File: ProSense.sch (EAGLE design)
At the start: 26 parts, among them U4 MIC2505 3.3

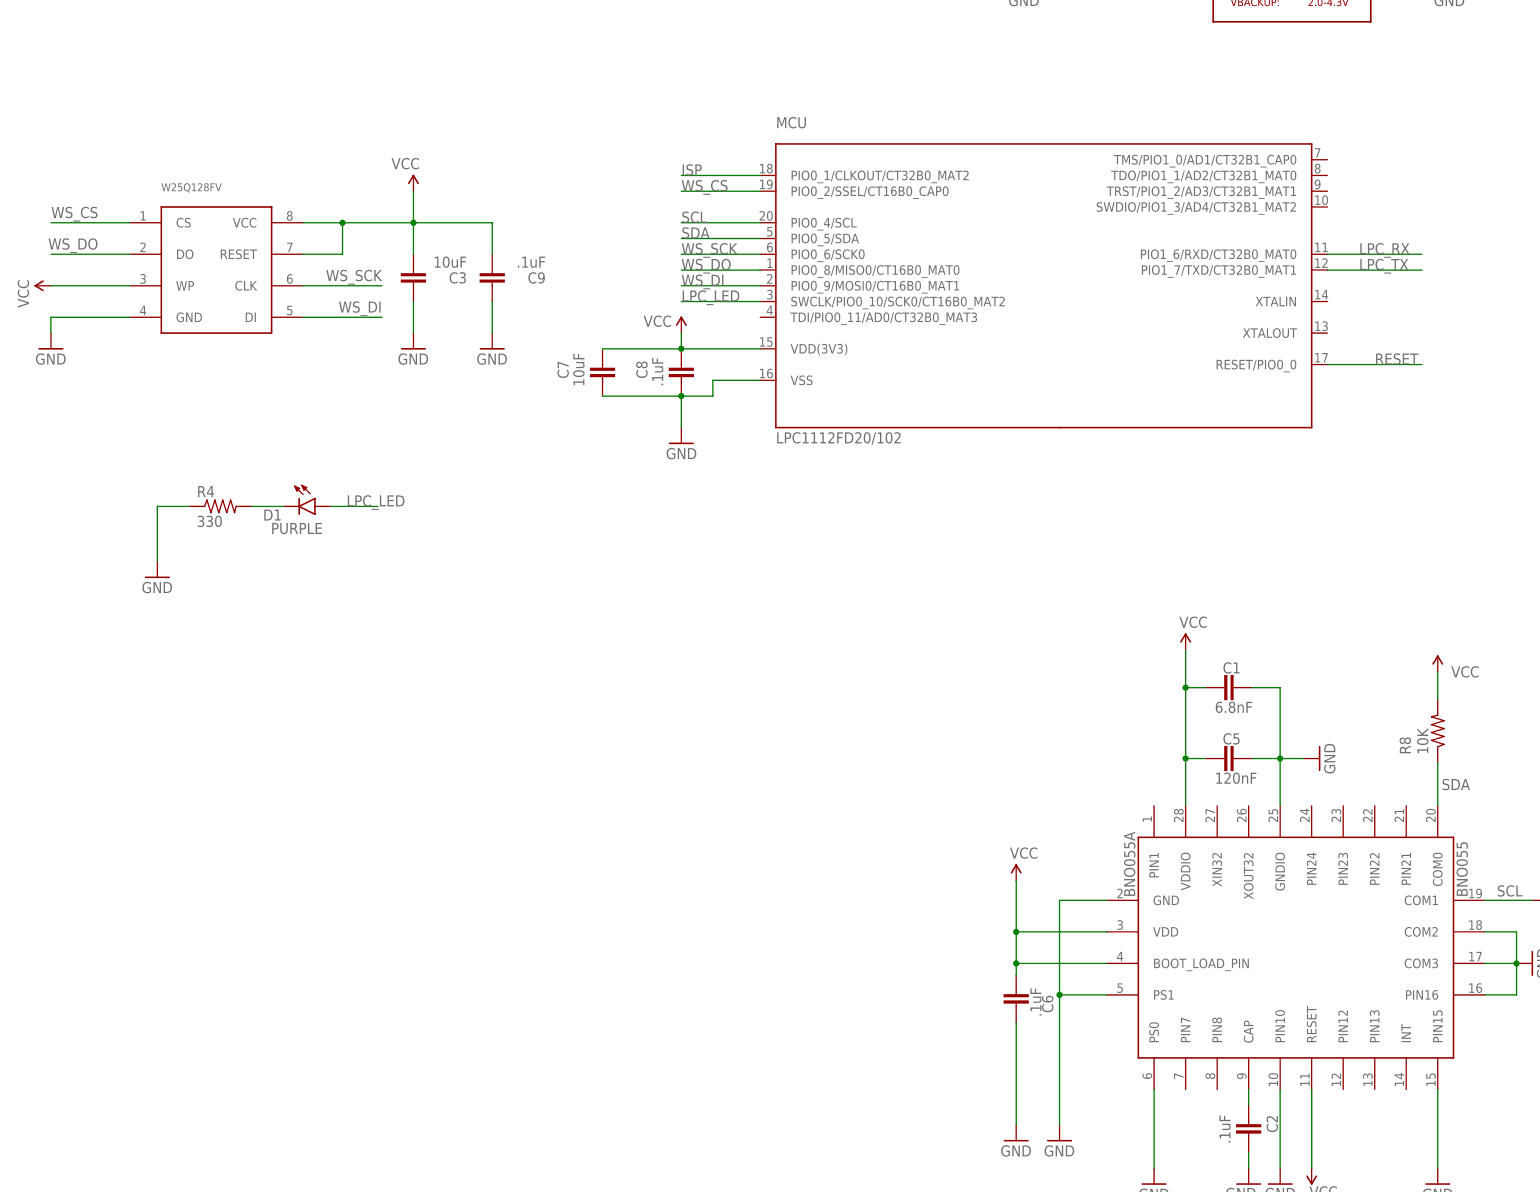
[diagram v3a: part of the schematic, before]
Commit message: Initial commit for QFN Package
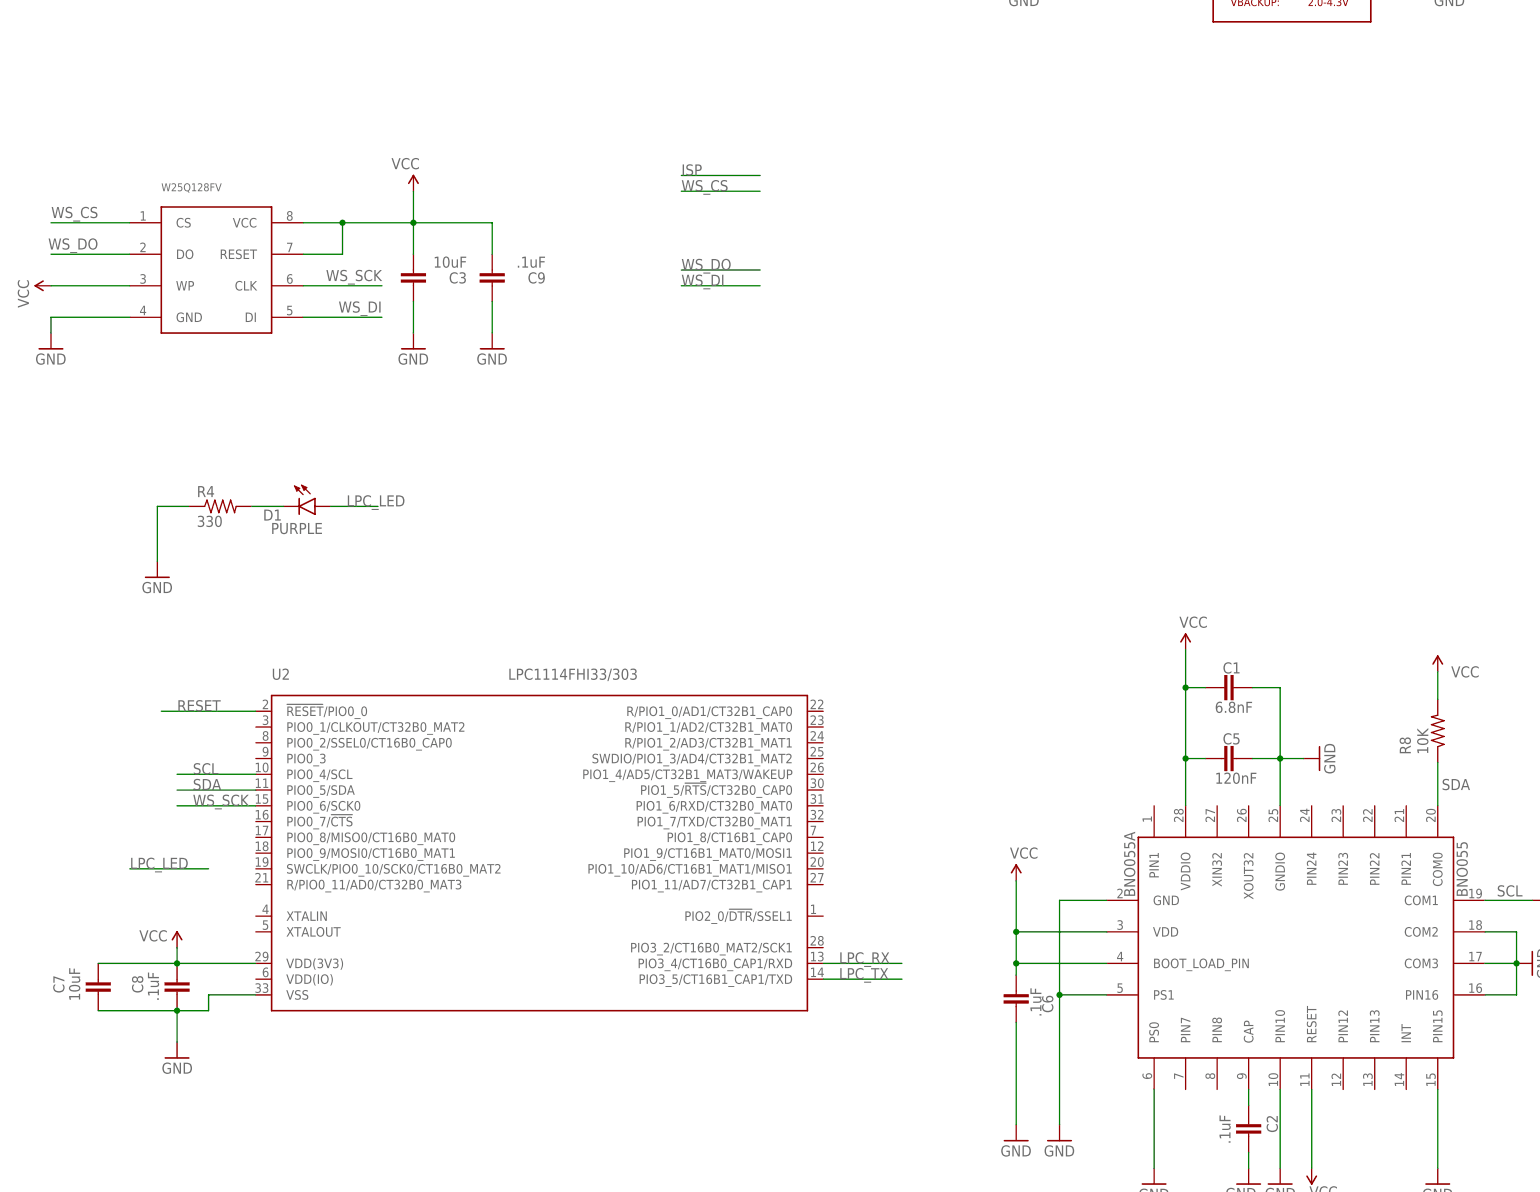
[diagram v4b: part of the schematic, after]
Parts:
- removed MCU: LPC1112FD20/102, NXP_60_26022015:LPC1112FD20/102
- added U2: LPC1114FHI33/303, NXP_60_26022015:LPC1114FHI33/303
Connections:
- net GND: now also U2.VSS; no longer MCU.VSS
- net ISP: no longer MCU.PIO0_1/CLKOUT/CT32B0_MAT2
- net LPC_LED: no longer MCU.SWCLK/PIO0_10/SCK0/CT16B0_MAT2
- net LPC_RX: now also U2.PIO3_4/CT16B0_CAP1/RXD; no longer MCU.PIO1_6/RXD/CT32B0_MAT0
- net LPC_TX: now also U2.PIO3_5/CT16B1_CAP1/TXD; no longer MCU.PIO1_7/TXD/CT32B0_MAT1
- net RESET: now also U2.!RESET!/PIO0_0; no longer MCU.RESET/PIO0_0
- net SCL: now also U2.PIO0_4/SCL; no longer MCU.PIO0_4/SCL
- net SDA: now also U2.PIO0_5/SDA; no longer MCU.PIO0_5/SDA
- net VCC: now also U2.VDD(3V3); no longer MCU.VDD(3V3)
- net WS_CS: no longer MCU.PIO0_2/SSEL/CT16B0_CAP0
- net WS_DI: no longer MCU.PIO0_9/MOSI0/CT16B0_MAT1
- net WS_DO: no longer MCU.PIO0_8/MISO0/CT16B0_MAT0
- net WS_SCK: now also U2.PIO0_6/SCK0; no longer MCU.PIO0_6/SCK0
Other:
- moved on the sheet: C7, C8
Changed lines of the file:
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@@
 <setting verticaltext="up"/>
 </settings>
-<grid distance="0.005" unitdist="inch" unit="inch" style="lines" multiple="1" display="no" altdistance="0.01" altunitdist="inch" altunit="inch"/>
+<grid distance="0.1" unitdist="inch" unit="inch" style="lines" multiple="1" display="no" altdistance="0.01" altunitdist="inch" altunit="inch"/>
 <layers>
 <layer number="1" name="Top" color="4" fill="1" visible="no" active="no"/>
@@
 <part name="SUPPLY1" library="SparkFun-Aesthetics" deviceset="V_BATT" device=""/>
 <part name="SUPPLY18" library="SparkFun-Aesthetics" deviceset="VCC" device=""/>
-<part name="MCU" library="NXP_60_26022015" deviceset="LPC1112FD20" device="" technology="/102"/>
 <part name="GND7" library="SparkFun-Aesthetics" deviceset="GND" device=""/>
 <part name="SUPPLY13" library="SparkFun-Aesthetics" deviceset="VCC" device=""/>
@@
 <part name="C9" library="SparkFun-Passives" deviceset="CAP" device="0805" value=".1uF"/>
 <part name="GND12" library="SparkFun-Aesthetics" deviceset="GND" device=""/>
+<part name="U2" library="NXP_60_26022015" deviceset="LPC1114FHI33/303" device=""/>
 </parts>
 <sheets>
@@
 <attribute name="VALUE" x="85.979" y="45.339" size="1.778" layer="96" rot="MR180"/>
 </instance>
-<instance part="C8" gate="G$1" x="-38.1" y="91.44" smashed="yes" rot="MR0">
-<attribute name="NAME" x="-45.339" y="91.694" size="1.778" layer="95" rot="MR90"/>
-<attribute name="VALUE" x="-42.799" y="90.424" size="1.778" layer="96" rot="MR90"/>
-</instance>
-<instance part="GND28" gate="1" x="-38.1" y="81.28" rot="MR0"/>
-<instance part="SUPPLY9" gate="G$1" x="-38.1" y="99.06" smashed="yes" rot="MR0">
-<attribute name="VALUE" x="-39.624" y="100.076" size="1.778" layer="96" rot="MR0"/>
+<instance part="C8" gate="G$1" x="-119.38" y="-7.62" smashed="yes" rot="MR0">
+<attribute name="NAME" x="-126.619" y="-7.366" size="1.778" layer="95" rot="MR90"/>
+<attribute name="VALUE" x="-124.079" y="-8.636" size="1.778" layer="96" rot="MR90"/>
+</instance>
+<instance part="GND28" gate="1" x="-119.38" y="-17.78" rot="MR0"/>
+<instance part="SUPPLY9" gate="G$1" x="-119.38" y="0" smashed="yes" rot="MR0">
+<attribute name="VALUE" x="-120.904" y="1.016" size="1.778" layer="96" rot="MR0"/>
 </instance>
 <instance part="SUPPLY11" gate="G$1" x="-81.28" y="121.92" rot="MR0"/>
@@
 <instance part="SUPPLY1" gate="G$1" x="154.94" y="81.28"/>
 <instance part="SUPPLY18" gate="G$1" x="-139.7" y="106.68" rot="MR270"/>
-<instance part="MCU" gate="G$1" x="20.32" y="106.68"/>
 <instance part="GND7" gate="1" x="-46.355" y="163.195" smashed="yes">
 <attribute name="VALUE" x="-48.895" y="161.29" size="1.27" layer="96"/>
@@
 </instance>
 <instance part="SUPPLY7" gate="G$1" x="43.18" y="48.006"/>
-<instance part="C7" gate="G$1" x="-50.8" y="91.44" smashed="yes" rot="MR0">
-<attribute name="NAME" x="-58.039" y="91.694" size="1.778" layer="95" rot="MR90"/>
-<attribute name="VALUE" x="-55.499" y="90.424" size="1.778" layer="96" rot="MR90"/>
+<instance part="C7" gate="G$1" x="-132.08" y="-7.62" smashed="yes" rot="MR0">
+<attribute name="NAME" x="-139.319" y="-7.366" size="1.778" layer="95" rot="MR90"/>
+<attribute name="VALUE" x="-136.779" y="-8.636" size="1.778" layer="96" rot="MR90"/>
 </instance>
 <instance part="C9" gate="G$1" x="-68.58" y="109.22" smashed="yes" rot="R180">
@@
 </instance>
 <instance part="GND12" gate="1" x="-68.58" y="96.52"/>
+<instance part="U2" gate="G$1" x="-60.96" y="17.78"/>
 </instances>
 <busses>
@@
 </segment>
 <segment>
-<pinref part="MCU" gate="G$1" pin="VDD(3V3)"/>
-<wire x1="-25.4" y1="96.52" x2="-38.1" y2="96.52" width="0.1524" layer="91"/>
-<wire x1="-38.1" y1="96.52" x2="-38.1" y2="99.06" width="0.1524" layer="91"/>
+<wire x1="-106.68" y1="-2.54" x2="-119.38" y2="-2.54" width="0.1524" layer="91"/>
+<wire x1="-119.38" y1="-2.54" x2="-119.38" y2="0" width="0.1524" layer="91"/>
 <pinref part="SUPPLY9" gate="G$1" pin="VCC"/>
 <pinref part="C8" gate="G$1" pin="1"/>
-<junction x="-38.1" y="96.52"/>
+<junction x="-119.38" y="-2.54"/>
 <pinref part="C7" gate="G$1" pin="1"/>
-<wire x1="-50.8" y1="96.52" x2="-38.1" y2="96.52" width="0.1524" layer="91"/>
+<wire x1="-132.08" y1="-2.54" x2="-119.38" y2="-2.54" width="0.1524" layer="91"/>
+<pinref part="U2" gate="G$1" pin="VDD(3V3)"/>
 </segment>
 <segment>
@@
 </segment>
 <segment>
-<pinref part="MCU" gate="G$1" pin="VSS"/>
-<wire x1="-25.4" y1="91.44" x2="-33.02" y2="91.44" width="0.1524" layer="91"/>
-<wire x1="-33.02" y1="91.44" x2="-33.02" y2="88.9" width="0.1524" layer="91"/>
+<wire x1="-106.68" y1="-7.62" x2="-114.3" y2="-7.62" width="0.1524" layer="91"/>
+<wire x1="-114.3" y1="-7.62" x2="-114.3" y2="-10.16" width="0.1524" layer="91"/>
 <pinref part="C8" gate="G$1" pin="2"/>
-<wire x1="-33.02" y1="88.9" x2="-38.1" y2="88.9" width="0.1524" layer="91"/>
+<wire x1="-114.3" y1="-10.16" x2="-119.38" y2="-10.16" width="0.1524" layer="91"/>
 <pinref part="GND28" gate="1" pin="GND"/>
-<wire x1="-38.1" y1="88.9" x2="-38.1" y2="83.82" width="0.1524" layer="91"/>
-<junction x="-38.1" y="88.9"/>
+<wire x1="-119.38" y1="-10.16" x2="-119.38" y2="-15.24" width="0.1524" layer="91"/>
+<junction x="-119.38" y="-10.16"/>
 <pinref part="C7" gate="G$1" pin="2"/>
-<wire x1="-50.8" y1="88.9" x2="-38.1" y2="88.9" width="0.1524" layer="91"/>
+<wire x1="-132.08" y1="-10.16" x2="-119.38" y2="-10.16" width="0.1524" layer="91"/>
+<pinref part="U2" gate="G$1" pin="VSS"/>
 </segment>
 <segment>
@@
 <net name="SDA" class="0">
 <segment>
-<pinref part="MCU" gate="G$1" pin="PIO0_5/SDA"/>
-<wire x1="-25.4" y1="114.3" x2="-38.1" y2="114.3" width="0.1524" layer="91"/>
-<label x="-38.1" y="114.3" size="1.778" layer="95"/>
+<wire x1="-106.68" y1="25.4" x2="-119.38" y2="25.4" width="0.1524" layer="91"/>
+<label x="-116.84" y="25.4" size="1.778" layer="95"/>
+<pinref part="U2" gate="G$1" pin="PIO0_5/SDA"/>
 </segment>
 <segment>
@@
 <net name="SCL" class="0">
 <segment>
-<pinref part="MCU" gate="G$1" pin="PIO0_4/SCL"/>
-<wire x1="-25.4" y1="116.84" x2="-38.1" y2="116.84" width="0.1524" layer="91"/>
-<label x="-38.1" y="116.84" size="1.778" layer="95"/>
+<wire x1="-106.68" y1="27.94" x2="-119.38" y2="27.94" width="0.1524" layer="91"/>
+<label x="-116.84" y="27.94" size="1.778" layer="95"/>
+<pinref part="U2" gate="G$1" pin="PIO0_4/SCL"/>
 </segment>
 <segment>
@@
 </segment>
 <segment>
-<pinref part="MCU" gate="G$1" pin="PIO1_6/RXD/CT32B0_MAT0"/>
-<wire x1="66.04" y1="111.76" x2="81.28" y2="111.76" width="0.1524" layer="91"/>
-<label x="71.12" y="111.76" size="1.778" layer="95"/>
+<wire x1="-15.24" y1="-2.54" x2="-2.54" y2="-2.54" width="0.1524" layer="91"/>
+<label x="-12.7" y="-2.54" size="1.778" layer="95"/>
+<pinref part="U2" gate="G$1" pin="PIO3_4/CT16B0_CAP1/RXD"/>
 </segment>
 </net>
@@
 </segment>
 <segment>
-<pinref part="MCU" gate="G$1" pin="PIO1_7/TXD/CT32B0_MAT1"/>
-<wire x1="66.04" y1="109.22" x2="81.28" y2="109.22" width="0.1524" layer="91"/>
-<label x="71.12" y="109.22" size="1.778" layer="95"/>
+<wire x1="-15.24" y1="-5.08" x2="-2.54" y2="-5.08" width="0.1524" layer="91"/>
+<label x="-12.7" y="-5.08" size="1.778" layer="95"/>
+<pinref part="U2" gate="G$1" pin="PIO3_5/CT16B1_CAP1/TXD"/>
 </segment>
 </net>
@@
 <net name="ISP" class="0">
 <segment>
-<pinref part="MCU" gate="G$1" pin="PIO0_1/CLKOUT/CT32B0_MAT2"/>
 <wire x1="-25.4" y1="124.46" x2="-38.1" y2="124.46" width="0.1524" layer="91"/>
 <label x="-38.1" y="124.46" size="1.778" layer="95"/>
@@
 <net name="RESET" class="0">
 <segment>
-<pinref part="MCU" gate="G$1" pin="RESET/PIO0_0"/>
-<wire x1="66.04" y1="93.98" x2="81.28" y2="93.98" width="0.1524" layer="91"/>
-<label x="73.66" y="93.98" size="1.778" layer="95"/>
+<wire x1="-121.92" y1="38.1" x2="-106.68" y2="38.1" width="0.1524" layer="91"/>
+<label x="-119.38" y="38.1" size="1.778" layer="95"/>
+<pinref part="U2" gate="G$1" pin="!RESET!/PIO0_0"/>
 </segment>
 <segment>
@@
 </segment>
 <segment>
-<pinref part="MCU" gate="G$1" pin="PIO0_2/SSEL/CT16B0_CAP0"/>
 <wire x1="-25.4" y1="121.92" x2="-38.1" y2="121.92" width="0.1524" layer="91"/>
 <label x="-38.1" y="121.92" size="1.778" layer="95"/>
@@
 </segment>
 <segment>
-<pinref part="MCU" gate="G$1" pin="PIO0_8/MISO0/CT16B0_MAT0"/>
 <wire x1="-25.4" y1="109.22" x2="-38.1" y2="109.22" width="0.1524" layer="91"/>
 <label x="-38.1" y="109.22" size="1.778" layer="95"/>
@@
 </segment>
 <segment>
-<pinref part="MCU" gate="G$1" pin="PIO0_6/SCK0"/>
-<wire x1="-25.4" y1="111.76" x2="-38.1" y2="111.76" width="0.1524" layer="91"/>
-<label x="-38.1" y="111.76" size="1.778" layer="95"/>
+<wire x1="-106.68" y1="22.86" x2="-119.38" y2="22.86" width="0.1524" layer="91"/>
+<label x="-116.84" y="22.86" size="1.778" layer="95"/>
+<pinref part="U2" gate="G$1" pin="PIO0_6/SCK0"/>
 </segment>
 </net>
@@
 </segment>
 <segment>
-<pinref part="MCU" gate="G$1" pin="PIO0_9/MOSI0/CT16B0_MAT1"/>
 <wire x1="-25.4" y1="106.68" x2="-38.1" y2="106.68" width="0.1524" layer="91"/>
 <label x="-38.1" y="106.68" size="1.778" layer="95"/>
@@
 </segment>
 <segment>
-<pinref part="MCU" gate="G$1" pin="SWCLK/PIO0_10/SCK0/CT16B0_MAT2"/>
-<wire x1="-25.4" y1="104.14" x2="-38.1" y2="104.14" width="0.1524" layer="91"/>
-<label x="-38.1" y="104.14" size="1.778" layer="95"/>
-</segment>
-</net>
+<wire x1="-114.3" y1="12.7" x2="-127" y2="12.7" width="0.1524" layer="91"/>
+<label x="-127" y="12.7" size="1.778" layer="95"/>
+</segment>
+</net>
